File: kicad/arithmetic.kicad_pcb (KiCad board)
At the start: 4 copper layers, 47.3 x 58.3 mm, 72 parts, among them J1 Conn_01x03_Male, J2 Conn_01x05_Male, J3 Conn_01x05_Male, J4 Conn_Coaxial, J5 Conn_Coaxial, J6 Conn_Coaxial, M2.5 MountingHole_2.7mm_M2.5_ISO73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, U1 LM317, U2 LM337, U3 OPA197xDBV, U4 OPA197xDBV, U5 OPA197xDBV

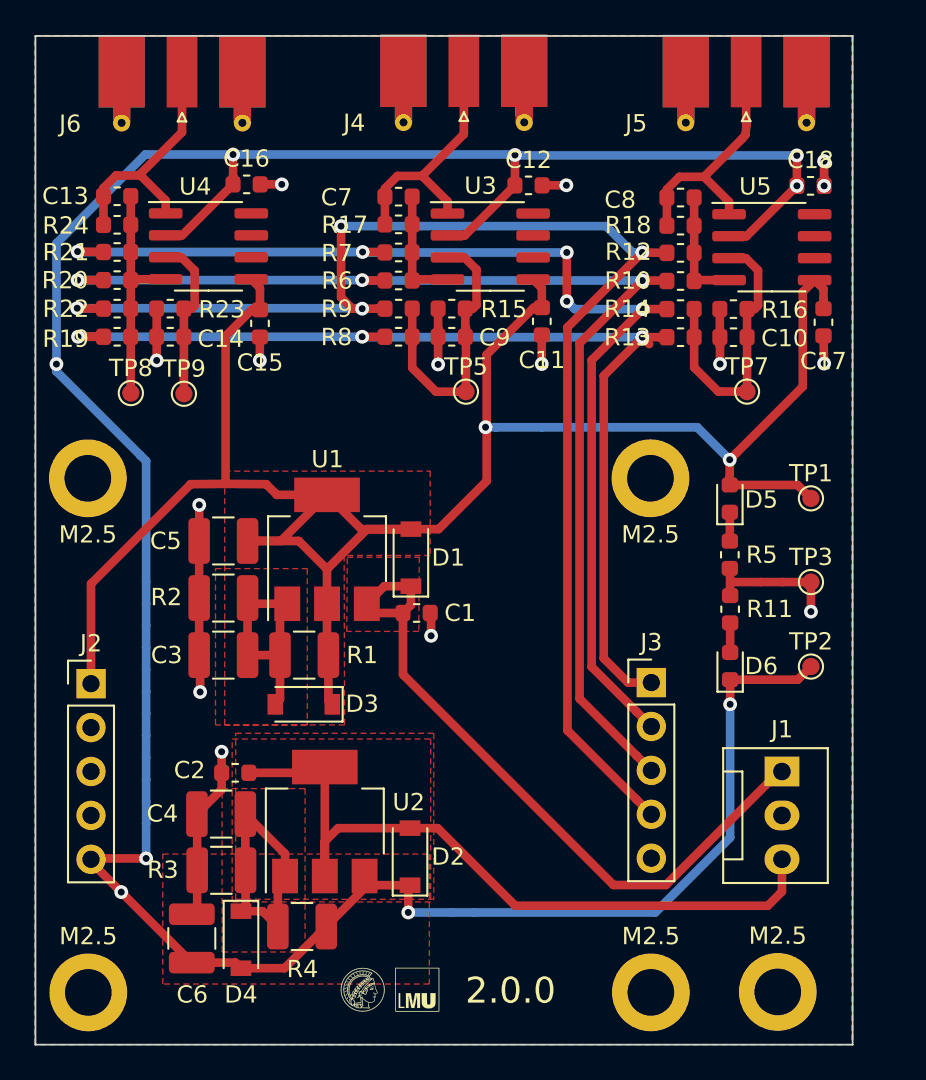
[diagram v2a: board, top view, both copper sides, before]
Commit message: amended OPA197 for SOIC8 pin layout
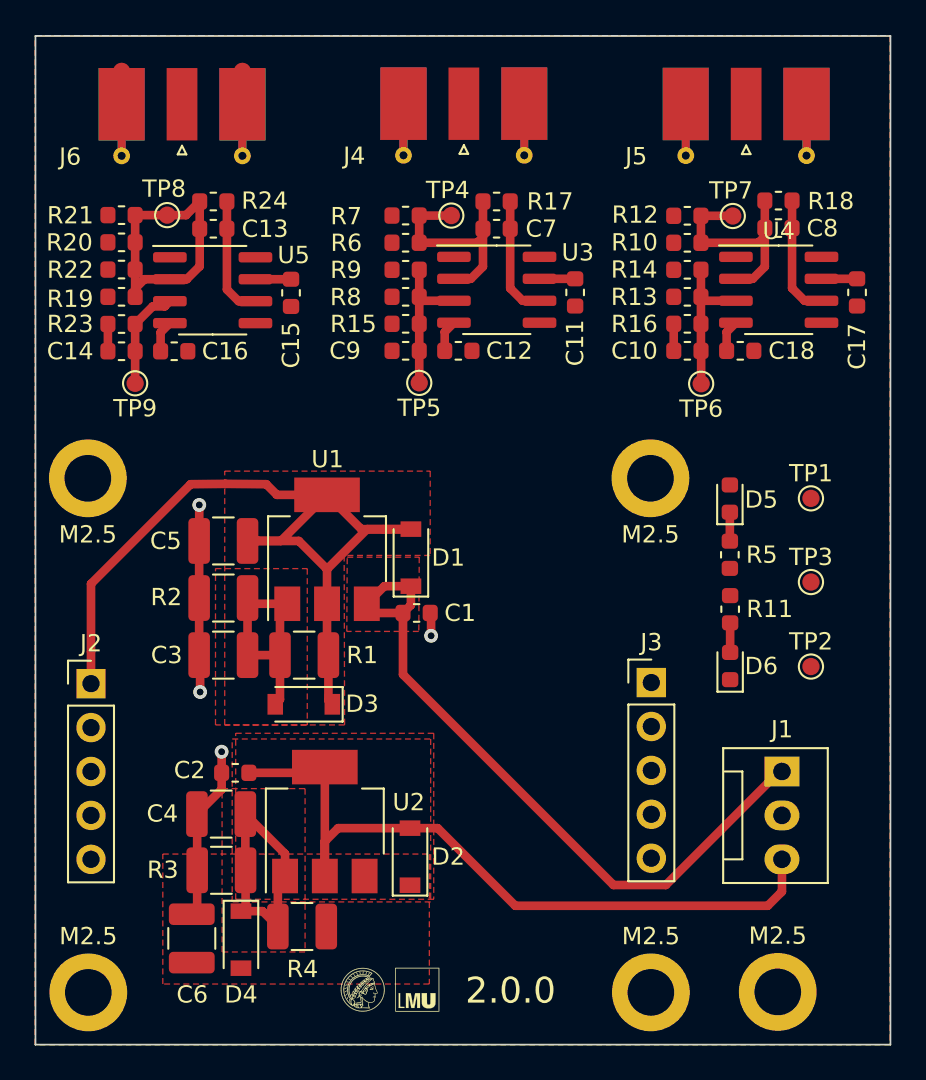
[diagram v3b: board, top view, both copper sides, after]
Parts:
- added TP4: DIFFX-, TestPoint:TestPoint_Pad_D1.0mm, F.Cu at (97.8, 87.9)
- added TP6: DIFFY+, TestPoint:TestPoint_Pad_D1.0mm, F.Cu at (112.3, 97.6)
- U3, U4, U5: value OPA197xDBV -> OPA197xD
- moved U4 33.1 mm to (116.8, 92.2)
- moved U5 32.4 mm to (84.0, 92.2)
- moved C16 10.5 mm to (81.8, 95.7)
- moved TP8 10.5 mm to (81.4, 87.9)
- moved C12 10.4 mm to (98.2, 95.7)
- moved C18 10.4 mm to (114.5, 95.7)
- moved TP7 10.2 mm to (114.1, 87.9)
- moved C7 5.97 mm to (100.4, 88.6), turned to 180 degrees
- moved C8 5.93 mm to (116.7, 88.6), turned to 180 degrees
- moved C13 5.87 mm to (84.0, 88.6), turned to 180 degrees
- moved R18 5.85 mm to (116.7, 87.0), turned to 180 degrees
- moved R17 5.82 mm to (100.4, 87.1), turned to 180 degrees
- moved R24 5.72 mm to (84.0, 87.1), turned to 180 degrees
- moved R23 2.96 mm to (78.7, 94.2)
- moved C14 2.94 mm to (78.7, 95.7)
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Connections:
- TP7 pad 1: Net-(C10-Pad2) -> Net-(C8-Pad2)
- U3 pad 1: /DIFFX -> Net-(U3-Pad1)
- U3 pad 2: -12V -> Net-(C7-Pad2)
- U3 pad 4: Net-(C7-Pad2) -> -12V
- U3 pad 5: +12V -> Net-(U3-Pad5)
- U3 pad 6: (no net) -> /DIFFX
- U3 pad 7: (no net) -> +12V
- U3 pad 8: (no net) -> Net-(U3-Pad8)
- U4 pad 1: /SUM -> Net-(U4-Pad1)
- U4 pad 2: -12V -> Net-(C8-Pad2)
- U4 pad 3: Net-(C14-Pad2) -> Net-(C10-Pad2)
- U4 pad 4: Net-(C13-Pad2) -> -12V
- U4 pad 5: +12V -> Net-(U4-Pad5)
- U4 pad 6: (no net) -> /DIFFY
- U4 pad 7: (no net) -> +12V
- U4 pad 8: (no net) -> Net-(U4-Pad8)
- U5 pad 1: /DIFFY -> Net-(U5-Pad1)
- U5 pad 2: -12V -> Net-(C13-Pad2)
- U5 pad 3: Net-(C10-Pad2) -> Net-(C14-Pad2)
- U5 pad 4: Net-(C8-Pad2) -> -12V
- U5 pad 5: +12V -> Net-(U5-Pad5)
- U5 pad 6: (no net) -> /SUM
- U5 pad 7: (no net) -> +12V
- U5 pad 8: (no net) -> Net-(U5-Pad8)
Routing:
- net -12V: track 166.8 -> 5.54 mm, vias 9 -> 0
- net /-Y2: track 80.8 -> 0.00 mm, vias 4 -> 0
- net GND: track 100.4 -> 31.5 mm, vias 15 -> 4
- net /-X2: track 68.5 -> 0.00 mm, vias 3 -> 0
- net /-Y1: track 66.8 -> 0.00 mm, vias 5 -> 0
- net +12V: track 120.4 -> 58.6 mm, vias 2 -> 0
- net /-X1: track 60.3 -> 0.00 mm, vias 3 -> 0
- net Net-(C9-Pad2): track 17.2 -> 8.64 mm
- net /DIFFX: track 14.4 -> 7.01 mm
- net /SUM: track 14.4 -> 7.02 mm
- net /DIFFY: track 14.4 -> 7.07 mm
- net Net-(C10-Pad2): track 16.0 -> 8.71 mm
- net Net-(C7-Pad2): track 6.92 -> 13.5 mm
- net Net-(C8-Pad2): track 6.87 -> 13.0 mm
- net Net-(C13-Pad2): track 13.4 -> 17.3 mm
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- removed copper zone on In1.Cu, net GND
- removed copper zone on In2.Cu, net GND
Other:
- board size 47.3 x 58.3 mm -> 49.5 x 58.3 mm

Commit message: re-routed traces on arithmetic board
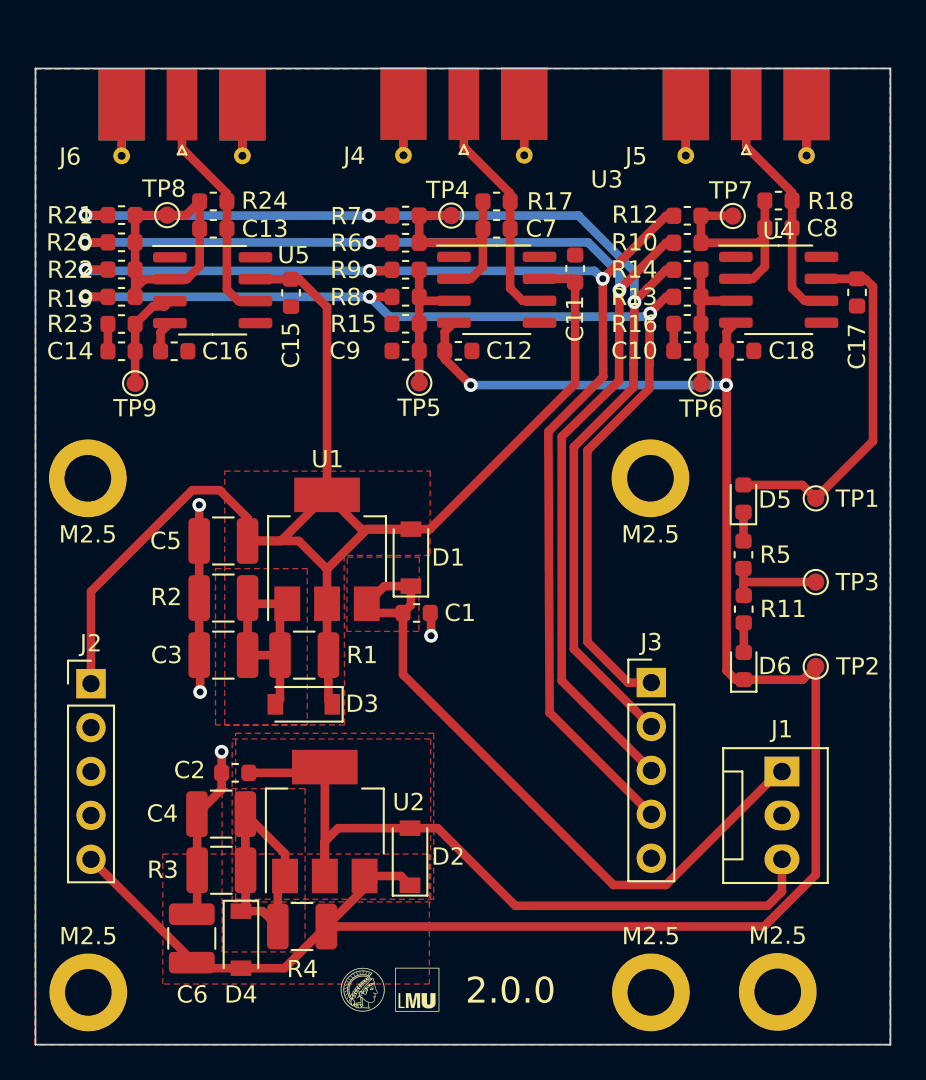
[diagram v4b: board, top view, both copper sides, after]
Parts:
- moved C11 1.37 mm to (105.0, 91.0), turned to 270 degrees
- moved D5 0.79 mm to (114.7, 104.3)
- moved D6 0.79 mm to (114.7, 113.9)
- moved R11 0.79 mm to (114.7, 110.7)
- moved R5 0.79 mm to (114.7, 107.5)
- moved TP1 0.28 mm to (118.9, 104.2)
- moved TP2 0.28 mm to (118.9, 114.0)
- moved TP3 0.28 mm to (118.9, 109.1)
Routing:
- net -12V: track 5.54 -> 112.9 mm, vias 0 -> 2
- net /-Y2: track 0.00 -> 73.2 mm, vias 0 -> 3
- net /-X2: track 0.00 -> 70.9 mm, vias 0 -> 3
- net /-Y1: track 0.00 -> 68.5 mm, vias 0 -> 3
- net /-X1: track 0.00 -> 63.0 mm, vias 0 -> 3
- net +12V: track 58.6 -> 107.2 mm
- net GND: track 31.5 -> 49.2 mm
- net /DIFFX: track 7.01 -> 13.8 mm
- net /SUM: track 7.02 -> 13.7 mm
- net /DIFFY: track 7.07 -> 13.8 mm
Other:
- board size 49.5 x 58.3 mm -> 49.5 x 56.5 mm

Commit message: move detector power supplies around (wip)
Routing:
- net GND: track 49.2 -> 51.9 mm, vias 4 -> 17

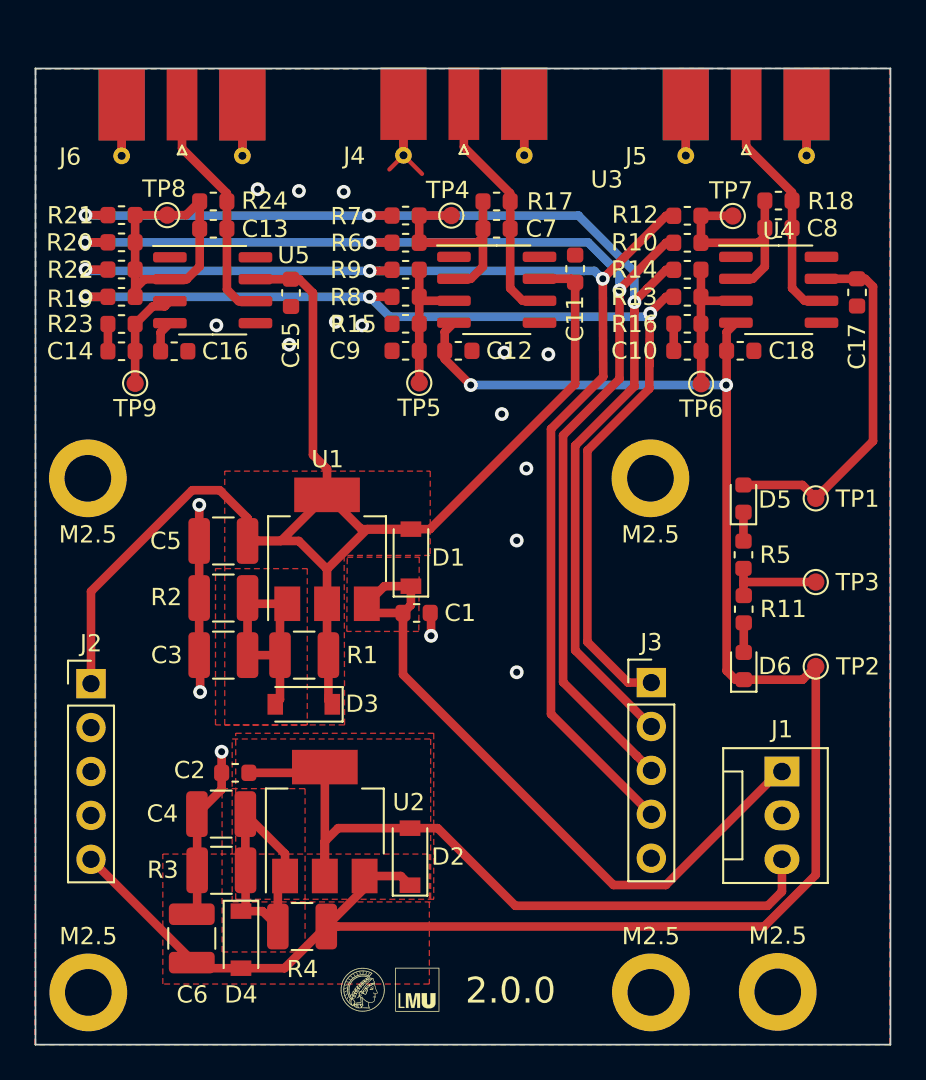
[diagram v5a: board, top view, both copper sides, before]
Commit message: added mounting holes to eeschema, replaced mounting holes with pad
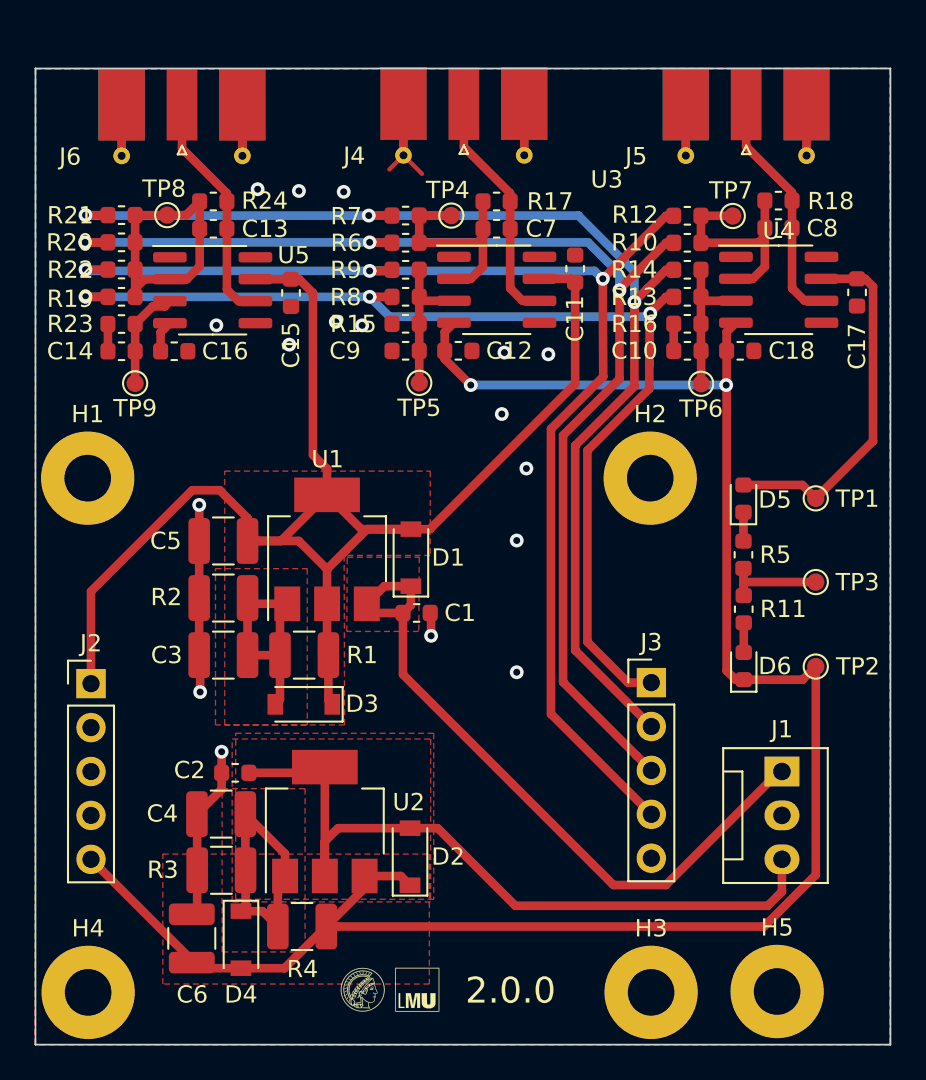
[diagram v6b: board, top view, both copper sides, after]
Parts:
- removed M2.5 (x5): MountingHole_2.7mm_M2.5_ISO7380_Pad, MountingHole:MountingHole_2.7mm_M2.5_ISO7380_Pad
- added H1: MountingHole_Pad, MountingHole:MountingHole_2.7mm_M2.5_Pad, F.Cu at (76.8, 103.1)
- added H2: MountingHole_Pad, MountingHole:MountingHole_2.7mm_M2.5_Pad, F.Cu at (109.3, 103.1)
- added H3: MountingHole_Pad, MountingHole:MountingHole_2.7mm_M2.5_Pad, F.Cu at (109.4, 132.8)
- added H4: MountingHole_Pad, MountingHole:MountingHole_2.7mm_M2.5_Pad, F.Cu at (76.8, 132.8)
- added H5: MountingHole_Pad, MountingHole:MountingHole_2.7mm_M2.5_Pad, F.Cu at (116.7, 132.8)

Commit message: changed header shield pins for improved detector routing
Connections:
- J2 pad 4: GND -> /-Y2
- J2 pad 5: -12V -> /-X1
- J3 pad 1: /-X1 -> -12V
- J3 pad 2: /-Y1 -> GND
- J3 pad 3: /-X2 -> GND
- J3 pad 4: /-Y2 -> /-X2
- J3 pad 5: GND -> /-Y1
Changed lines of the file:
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@@
     (fp_line (start -0.635 -1.27) (end 1.27 -1.27) (layer F.Fab) (width 0.1))
     (pad 5 thru_hole oval (at 0 10.16) (size 1.7 1.7) (drill 1) (layers *.Cu *.Mask)
+      (net 18 /-Y1))
+    (pad 4 thru_hole oval (at 0 7.62) (size 1.7 1.7) (drill 1) (layers *.Cu *.Mask)
+      (net 19 /-X2))
+    (pad 3 thru_hole oval (at 0 5.08) (size 1.7 1.7) (drill 1) (layers *.Cu *.Mask)
       (net 1 GND))
-    (pad 4 thru_hole oval (at 0 7.62) (size 1.7 1.7) (drill 1) (layers *.Cu *.Mask)
-      (net 17 /-Y2))
-    (pad 3 thru_hole oval (at 0 5.08) (size 1.7 1.7) (drill 1) (layers *.Cu *.Mask)
-      (net 19 /-X2))
     (pad 2 thru_hole oval (at 0 2.54) (size 1.7 1.7) (drill 1) (layers *.Cu *.Mask)
-      (net 18 /-Y1))
+      (net 1 GND))
     (pad 1 thru_hole rect (at 0 0) (size 1.7 1.7) (drill 1) (layers *.Cu *.Mask)
-      (net 20 /-X1))
+      (net 7 -12V))
     (model ${KISYS3DMOD}/Connector_PinHeader_2.54mm.3dshapes/PinHeader_1x05_P2.54mm_Vertical.wrl
       (at (xyz 0 0 0))
@@
     (fp_line (start -0.635 -1.27) (end 1.27 -1.27) (layer F.Fab) (width 0.1))
     (pad 5 thru_hole oval (at 0 10.16) (size 1.7 1.7) (drill 1) (layers *.Cu *.Mask)
-      (net 7 -12V))
+      (net 20 /-X1))
     (pad 4 thru_hole oval (at 0 7.62) (size 1.7 1.7) (drill 1) (layers *.Cu *.Mask)
-      (net 1 GND))
+      (net 17 /-Y2))
     (pad 3 thru_hole oval (at 0 5.08) (size 1.7 1.7) (drill 1) (layers *.Cu *.Mask)
       (net 1 GND))

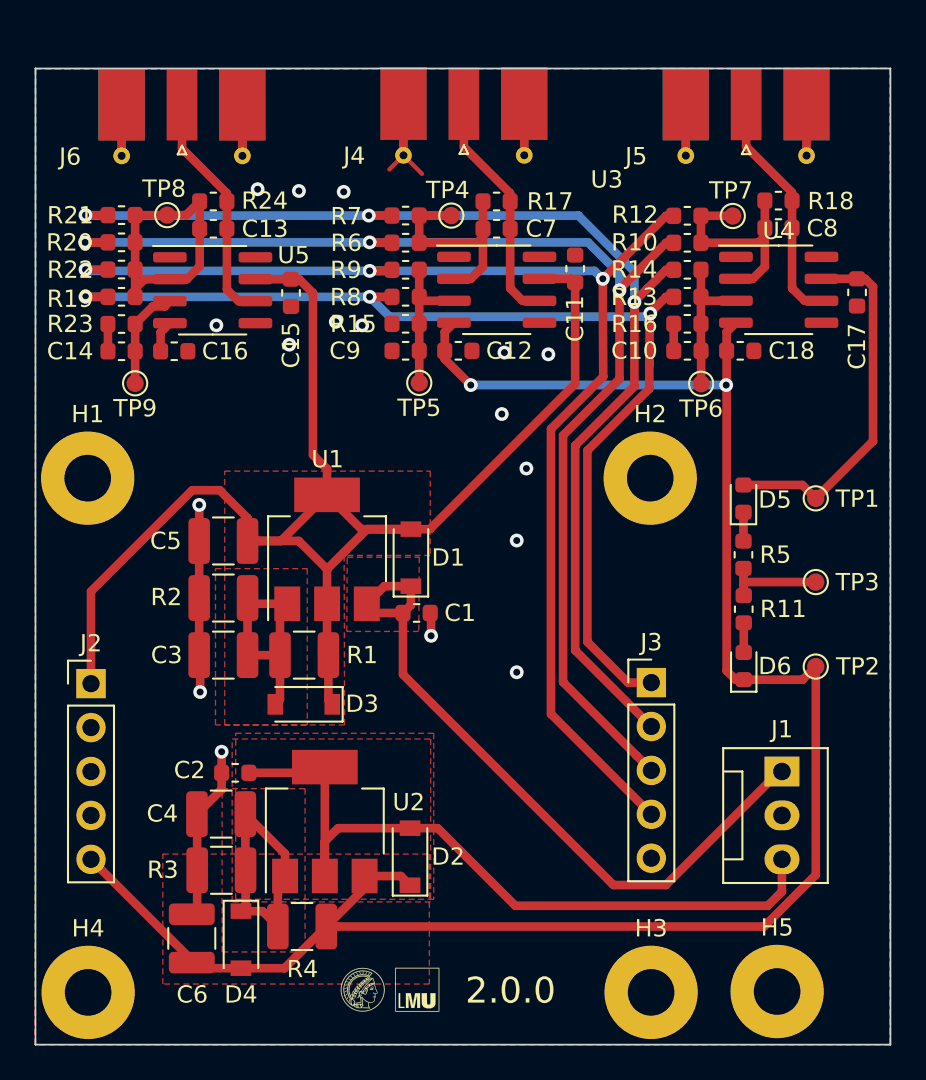
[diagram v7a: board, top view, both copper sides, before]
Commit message: adjusted arithmetic pcb for updated detector pcb
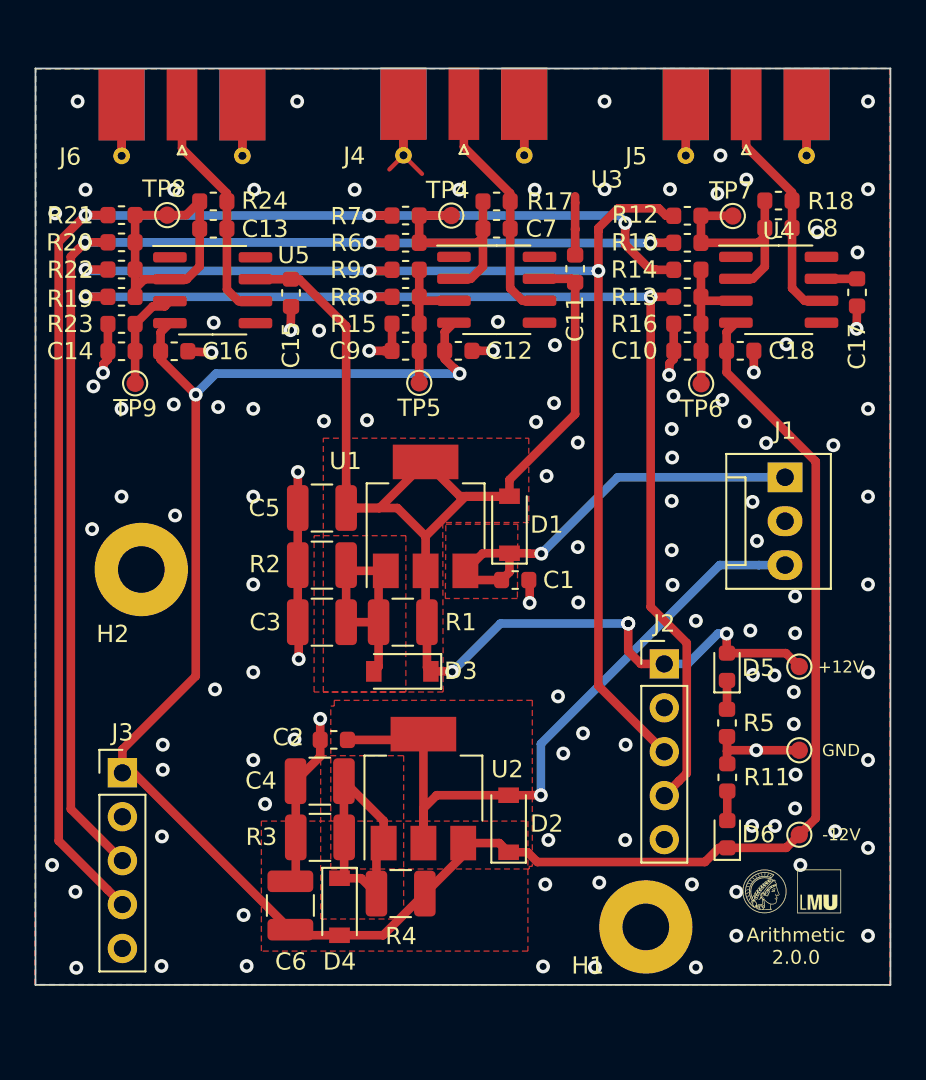
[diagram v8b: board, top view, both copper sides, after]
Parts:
- removed H3, H4, H5: MountingHole_Pad, MountingHole:MountingHole_2.7mm_M2.5_Pad
- moved H1 41.4 mm to (109.1, 129.0)
- moved J2 33.2 mm to (110.1, 113.8)
- moved J3 31.0 mm to (78.8, 120.1)
- moved H2 29.9 mm to (79.9, 108.4)
- moved G*** 23.9 mm to (117.6, 127.0)
- moved J1 17.0 mm to (117.1, 103.0)
- moved +12V 9.77 mm to (117.9, 114.0)
- moved D5 9.77 mm to (113.8, 114.0)
- moved D6 9.77 mm to (113.8, 123.7)
- moved R11 9.77 mm to (113.8, 120.4)
- moved R5 9.77 mm to (113.8, 117.2)
- moved -12V 9.77 mm to (117.9, 123.7)
- moved GND 9.77 mm to (117.9, 118.8)
- moved C4 6.01 mm to (90.2, 120.6)
- moved R1 6.01 mm to (95.0, 111.4)
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- renumbered TP1 to +12V, TP2 to -12V, TP3 to GND
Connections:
- H1 pad 1: GND -> (no net)
- H2 pad 1: GND -> (no net)
- J2 pad 3: GND -> /-Y2
- J2 pad 4: /-Y2 -> /-X1
- J2 pad 5: /-X1 -> GND
- J3 pad 3: GND -> /-X2
- J3 pad 4: /-X2 -> /-Y1
- J3 pad 5: /-Y1 -> GND
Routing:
- net GND: track 51.9 -> 68.3 mm, vias 17 -> 116
- net +15V: track 40.3 -> 24.8 mm, vias 0 -> 1
- net +12V: track 107.2 -> 92.0 mm, vias 0 -> 4
- net -12V: track 112.9 -> 127.4 mm
- net /-Y1: track 68.4 -> 80.9 mm
- net /-X1: track 63.0 -> 66.9 mm
- net /-Y2: track 73.1 -> 69.2 mm
- net /-X2: track 70.8 -> 74.1 mm
- net -15V: track 43.7 -> 41.3 mm, vias 0 -> 1
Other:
- board size 49.5 x 56.5 mm -> 49.5 x 53 mm
- copper layers 4 -> 2
- board text added: "Arithmetic 2.0.0"
- board text removed: "2.0.0"
